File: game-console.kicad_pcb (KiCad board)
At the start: 2 copper layers, 100 x 81 mm, 63 parts, among them IC1 MCP1700, IC2 78T, U5 DC IN

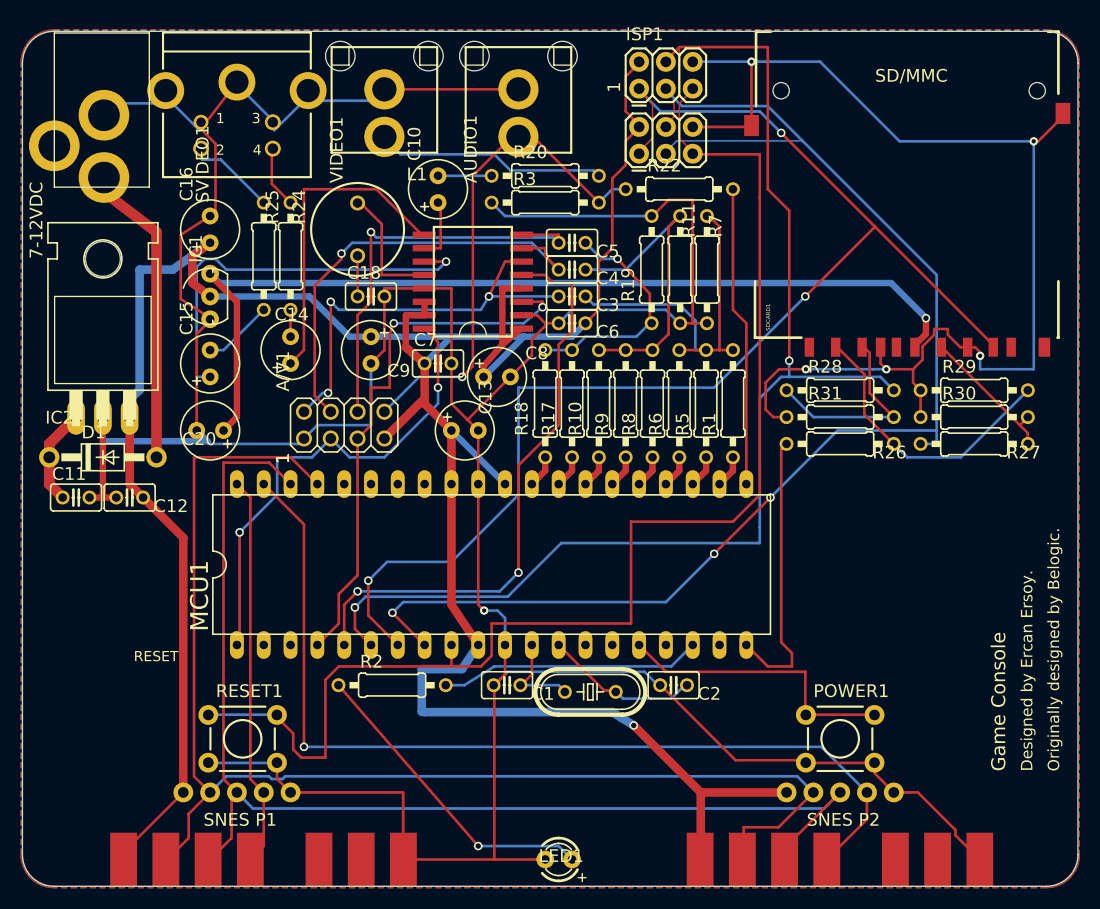
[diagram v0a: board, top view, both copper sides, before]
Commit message: Some updates
  * Remove old names
  * Update format of project files as new format
  * Remove old and garbage files
  * Update .gitignore

Signed-off-by: Ercan Ersoy <ercanersoy@ercanersoy.net>
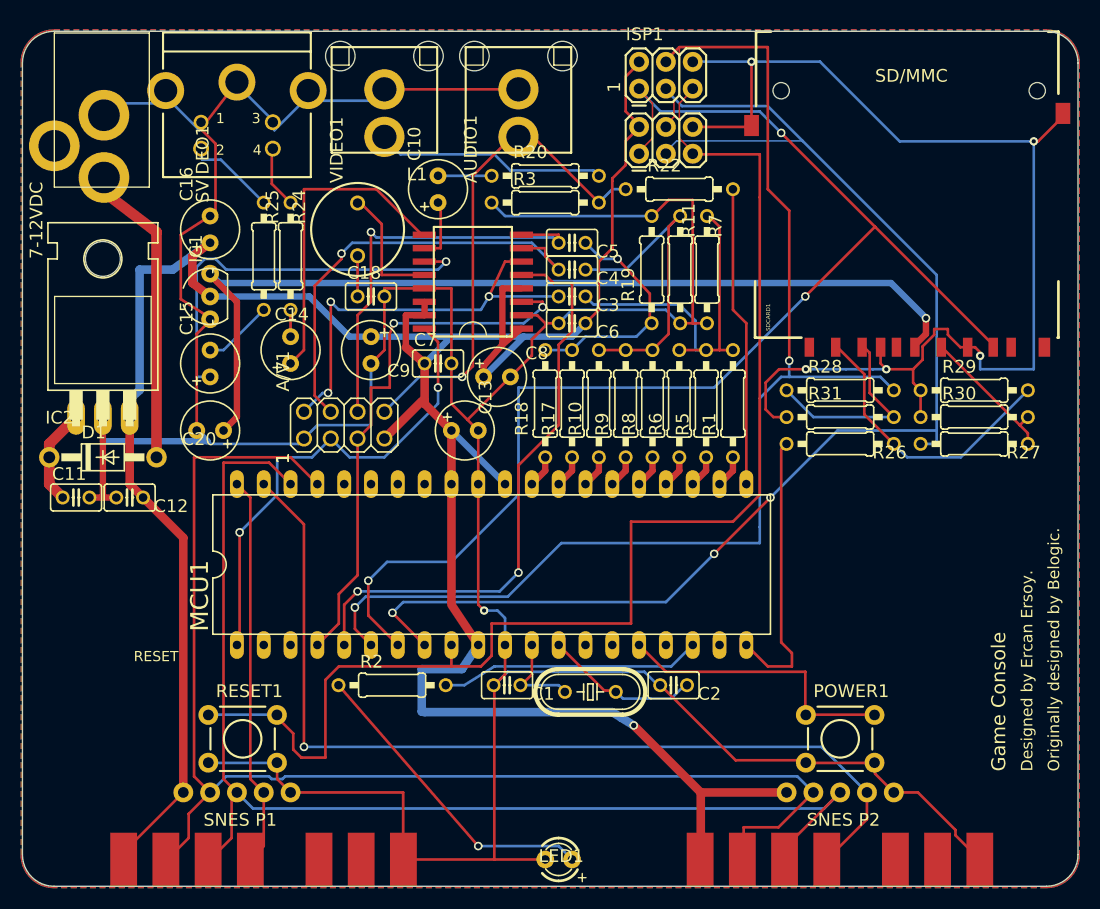
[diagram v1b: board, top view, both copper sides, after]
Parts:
- A/V1: footprint Uzebox Game Console F5:2X04 -> Game-Console:2X04
- AD725: footprint Uzebox Game Console F5:SO16W -> Game-Console:SO16W
- AUDIO1, VIDEO1: footprint Uzebox Game Console F5:RCA -> Game-Console:RCA
- C1, C11, C12, C18, C2, C3, C4, C5, C6, C7: footprint Uzebox Game Console F5:C025-025X050 -> Game-Console:C025-025X050
- C10, C13, C14, C15, C16, C20, C8, C9: footprint Uzebox Game Console F5:E2,5-6 -> Game-Console:E2,5-6
- D1: footprint Uzebox Game Console F5:DO41-10 -> Game-Console:DO41-10
- IC1: footprint Uzebox Game Console F5:TO92-INLINE -> Game-Console:TO92-INLINE
- IC2: footprint Uzebox Game Console F5:TO220H -> Game-Console:TO220H
- ISP-90DEG1, ISP1: footprint Uzebox Game Console F5:2X3 -> Game-Console:2X3
- JP4, JP5: footprint Uzebox Game Console F5:1X05 -> Game-Console:1X05
- L1: footprint Uzebox Game Console F5:6000-XXXX-RC -> Game-Console:6000-XXXX-RC
- LED1: footprint Uzebox Game Console F5:LED3MM -> Game-Console:LED3MM
- MCU1: footprint Uzebox Game Console F5:DIL40 -> Game-Console:DIL40
- POWER1, RESET1: footprint Uzebox Game Console F5:TACTILE-PTH -> Game-Console:TACTILE-PTH
- R1, R10, R11, R17, R18, R19, R2, R20, R22, R24, R25, R26, R27, R28, R29, R3, R30, R31, R5, R6, R7, R8, R9: footprint Uzebox Game Console F5:0207_10 -> Game-Console:0207_10
- SDCARD1: footprint Uzebox Game Console F5:SDCARD_4UCONN -> Game-Console:SDCARD_4UCONN
- SNES_P1, SNES_P2: footprint Uzebox Game Console F5:SNES_CONNECTOR -> Game-Console:SNES_CONNECTOR
- SVIDEO1: footprint Uzebox Game Console F5:MINIDIN4 -> Game-Console:MINIDIN4
- U5: footprint Uzebox Game Console F5:PJ-102A -> Game-Console:PJ-102A
- XTAL1: footprint Uzebox Game Console F5:HC49_S -> Game-Console:HC49_S
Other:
- net class Default removed
